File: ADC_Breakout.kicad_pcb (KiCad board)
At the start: 2 copper layers, 40.1 x 35.2 mm, 25 parts, among them J1 Analog Pins, J2 Digital Power, J3 Clock Chooser, J4 Analog Power, J5 SPI Communication, U1 ADS131M08QPBSRQ1, U2 SN74AUP2G80DCUR, X1 SIT8924BA-22-33E-8.192000, Y1 Crystal_Small

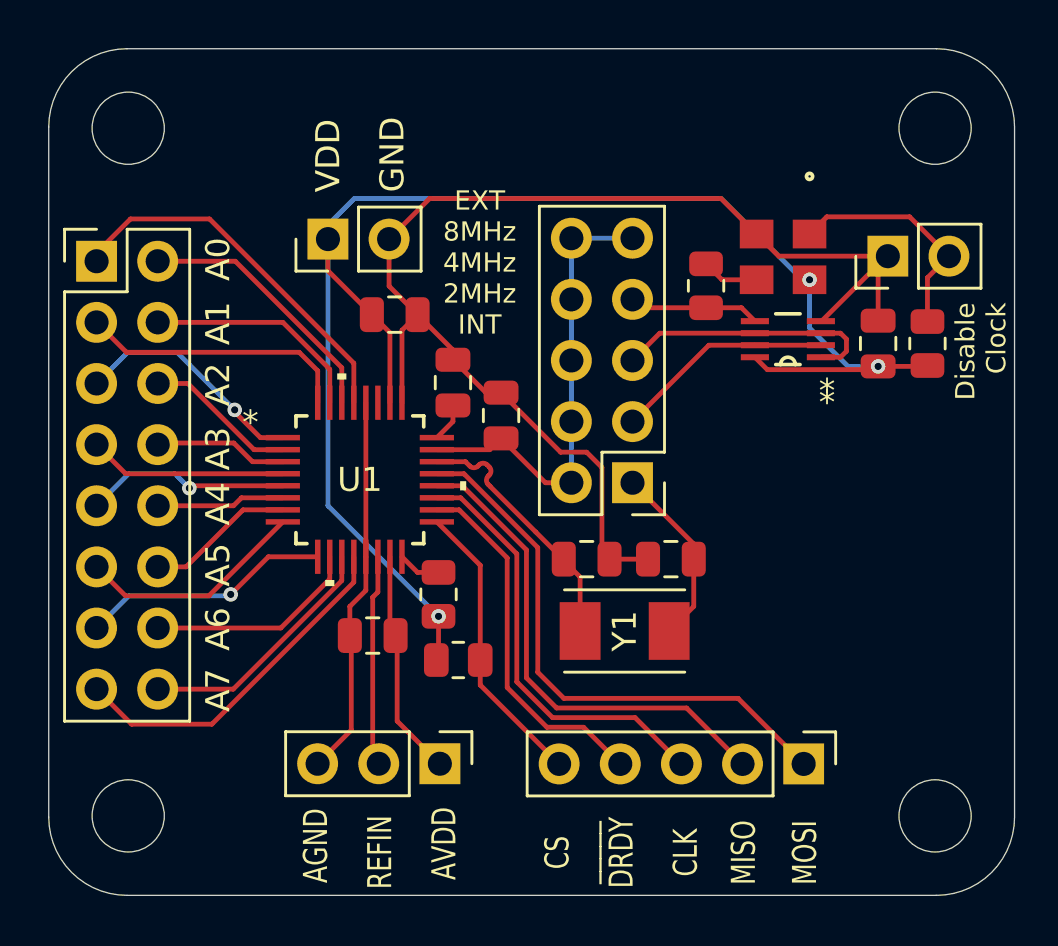
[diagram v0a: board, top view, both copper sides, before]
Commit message: Updated explanations for headers
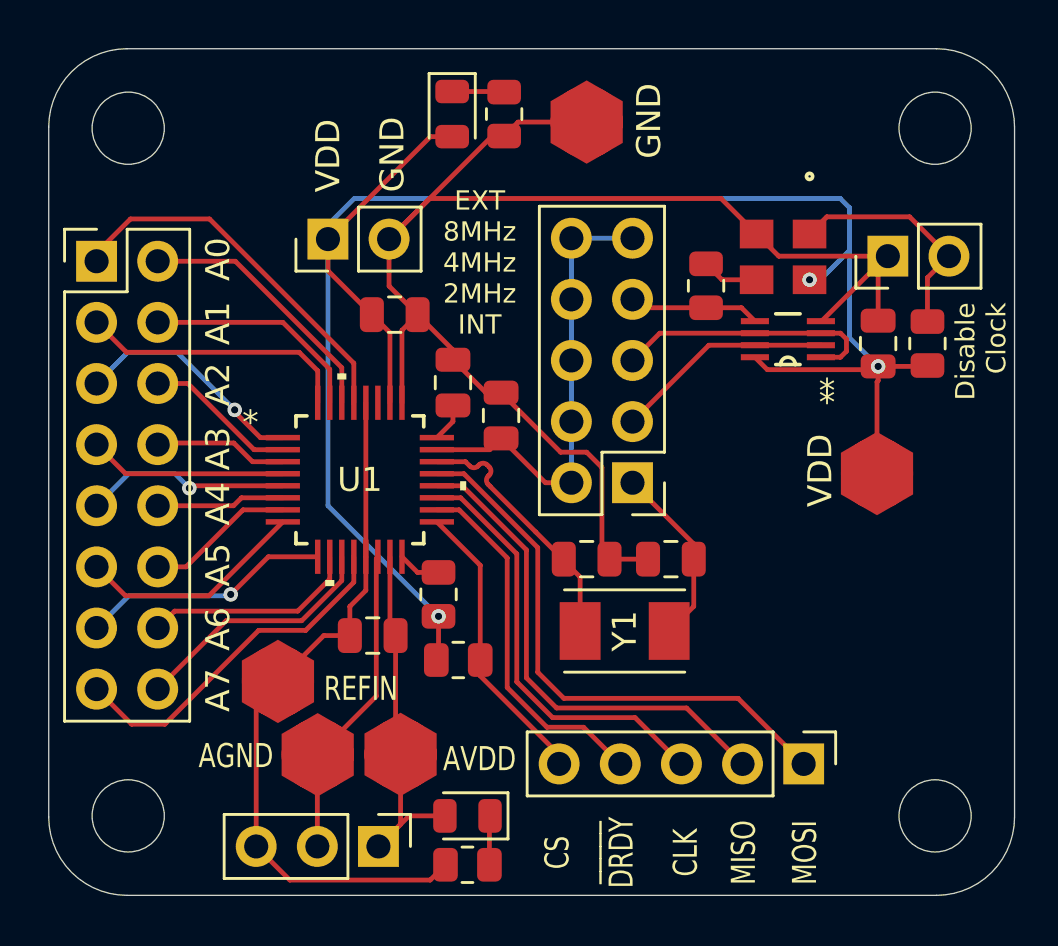
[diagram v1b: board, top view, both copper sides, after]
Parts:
- added D1: LED, LED_SMD:LED_0805_2012Metric, F.Cu at (40.8, 28.2)
- added D2: LED, LED_SMD:LED_0805_2012Metric, F.Cu at (41.4, 57.4)
- added R5: 500, Resistor_SMD:R_0805_2012Metric, F.Cu at (42.9, 28.2)
- added R6: 500, Resistor_SMD:R_0805_2012Metric, F.Cu at (41.4, 59.4)
- added TP1: TestPoint, SVT_Special:TestPoint_HEX_3mmID, F.Cu at (58.4, 43.2)
- added TP2: TestPoint, SVT_Special:TestPoint_HEX_3mmID, F.Cu at (38.6, 54.8)
- added TP3: TestPoint, SVT_Special:TestPoint_HEX_3mmID, F.Cu at (46.4, 28.6)
- added TP4: TestPoint, SVT_Special:TestPoint_HEX_3mmID, F.Cu at (33.5, 51.8)
- added TP5: TestPoint, SVT_Special:TestPoint_HEX_3mmID, F.Cu at (35.2, 54.9)
- moved J4 4.28 mm to (37.7, 58.7)
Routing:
- net VDD: track 62.7 -> 78.4 mm
- net GNDA: track 15.9 -> 29.7 mm
- net GND: track 52.8 -> 63.0 mm
- net VDDA: track 9.46 -> 15.9 mm
- net /REFIN: track 8.79 -> 13.1 mm
- net Net-(D1-K): track 0.00 -> 2.17 mm
- net Net-(D2-K): track 0.00 -> 2.04 mm

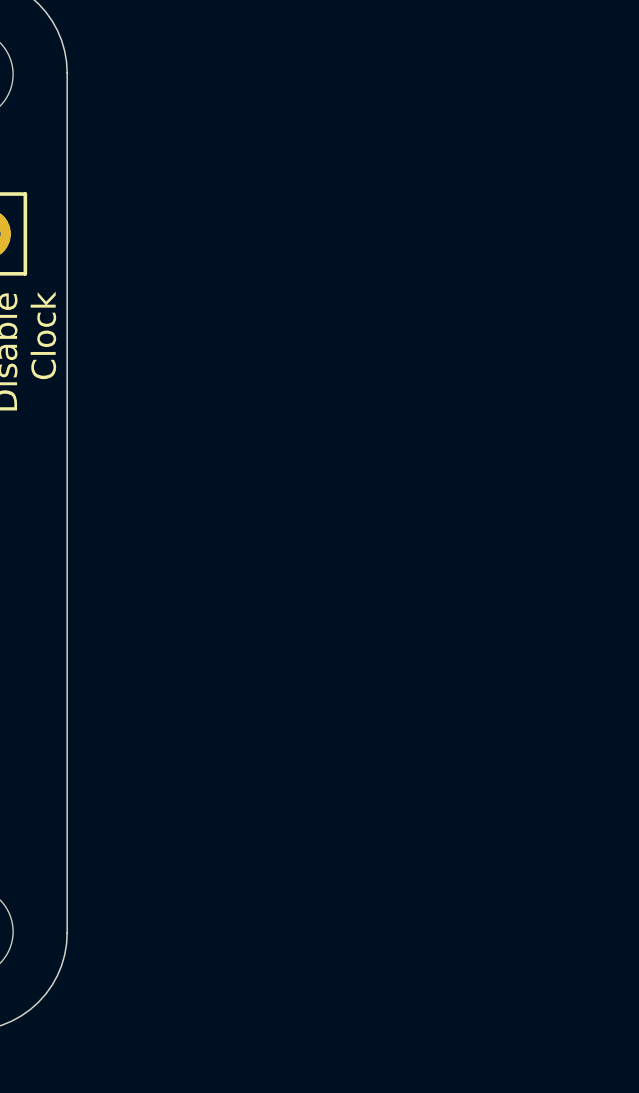
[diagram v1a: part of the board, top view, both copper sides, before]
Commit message: Updated schematic with antialiasing
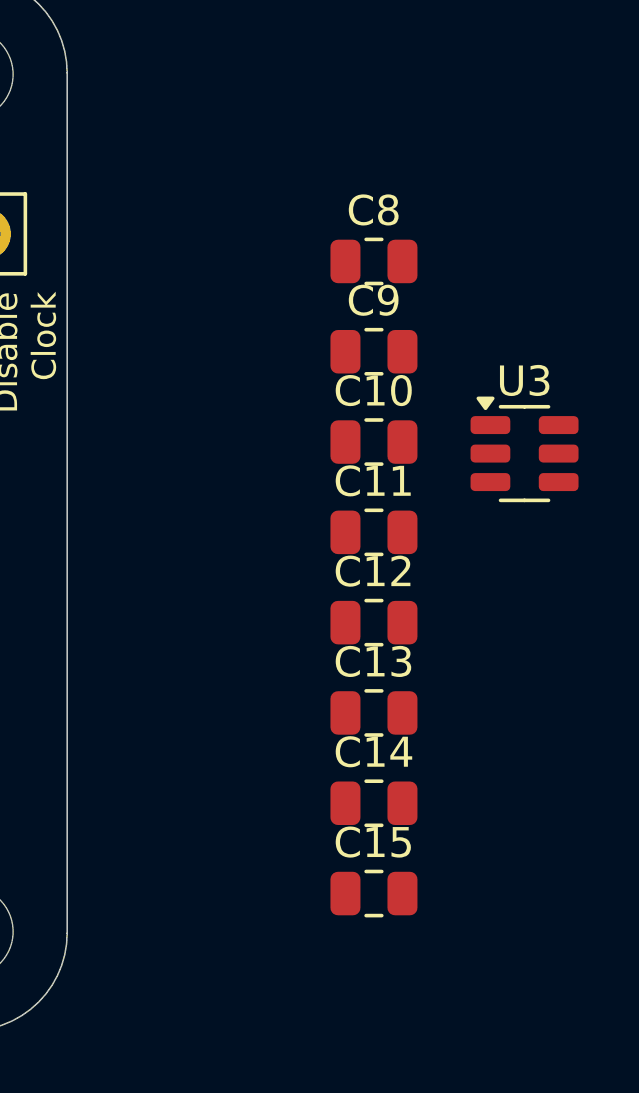
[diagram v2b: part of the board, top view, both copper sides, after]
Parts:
- added C10: 1000p, Capacitor_SMD:C_0805_2012Metric, F.Cu at (74.4, 41.1)
- added C11: 1000p, Capacitor_SMD:C_0805_2012Metric, F.Cu at (74.4, 44.1)
- added C12: 1000p, Capacitor_SMD:C_0805_2012Metric, F.Cu at (74.4, 47.1)
- added C13: 1000p, Capacitor_SMD:C_0805_2012Metric, F.Cu at (74.4, 50.1)
- added C14: 1000p, Capacitor_SMD:C_0805_2012Metric, F.Cu at (74.4, 53.1)
- added C15: 1000p, Capacitor_SMD:C_0805_2012Metric, F.Cu at (74.4, 56.1)
- added C8: 1000p, Capacitor_SMD:C_0805_2012Metric, F.Cu at (74.4, 35.1)
- added C9: 1000p, Capacitor_SMD:C_0805_2012Metric, F.Cu at (74.4, 38.1)
- added U3: WE-TVS-824015043, Package_TO_SOT_SMD:SOT-23-6, F.Cu at (79.4, 41.5)

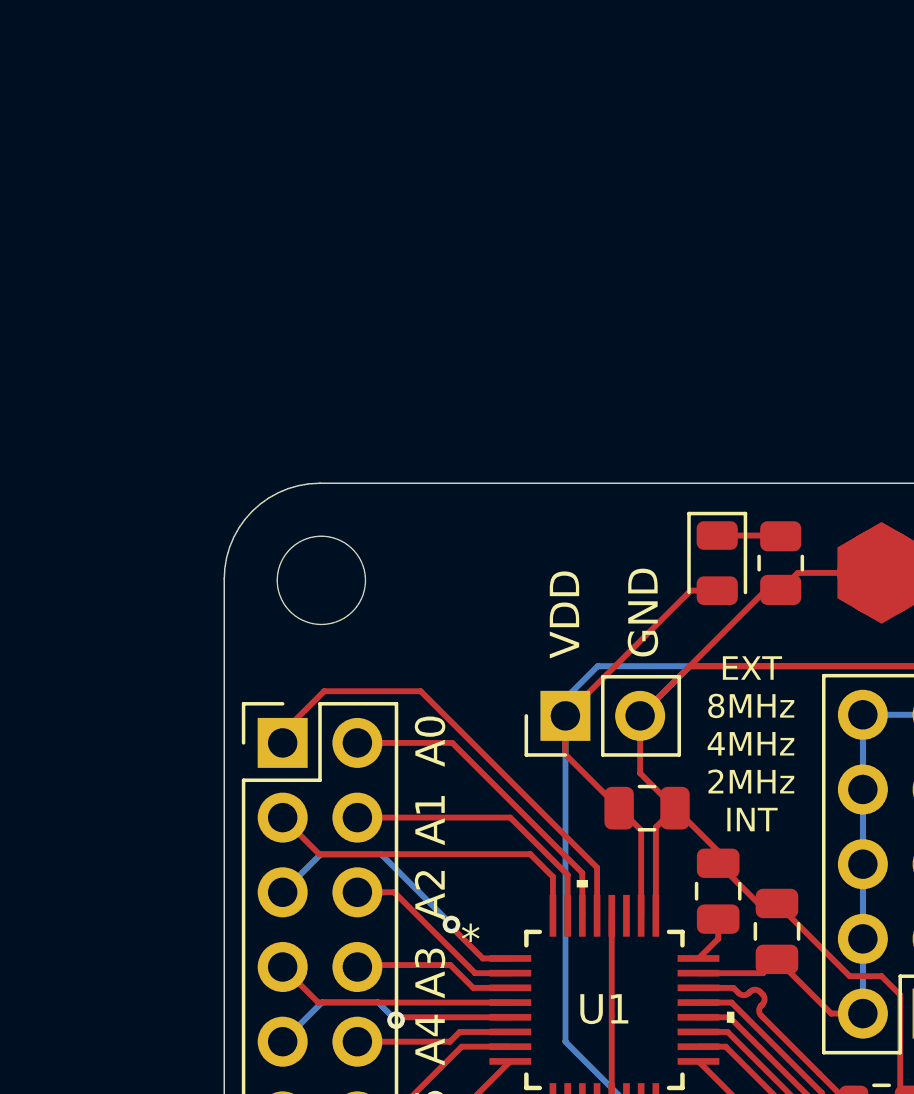
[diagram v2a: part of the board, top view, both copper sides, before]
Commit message: New footprints added
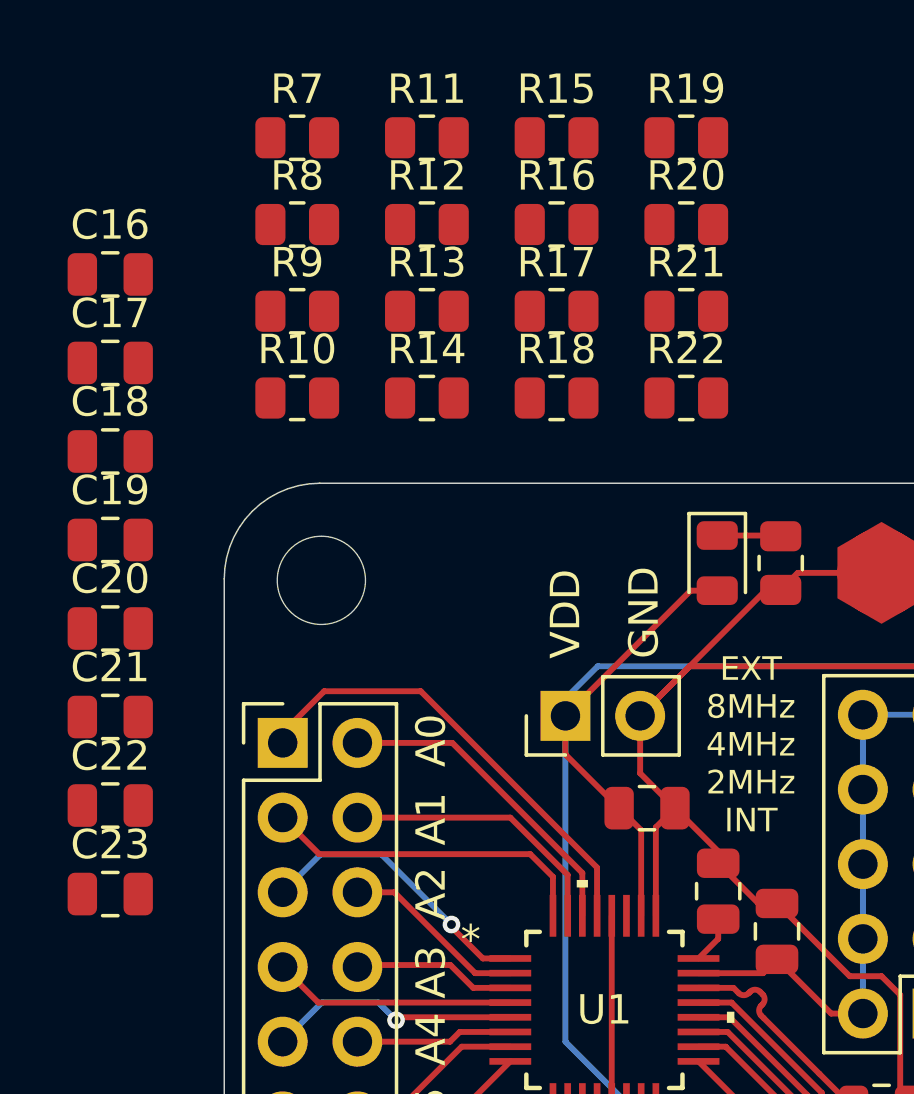
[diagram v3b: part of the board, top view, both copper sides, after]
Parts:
- added C16: 1000p, Capacitor_SMD:C_0805_2012Metric, F.Cu at (20.1, 18.4)
- added C17: 1000p, Capacitor_SMD:C_0805_2012Metric, F.Cu at (20.1, 21.4)
- added C18: 1000p, Capacitor_SMD:C_0805_2012Metric, F.Cu at (20.1, 24.4)
- added C19: 1000p, Capacitor_SMD:C_0805_2012Metric, F.Cu at (20.1, 27.5)
- added C20: 1000p, Capacitor_SMD:C_0805_2012Metric, F.Cu at (20.1, 30.5)
- added C21: 1000p, Capacitor_SMD:C_0805_2012Metric, F.Cu at (20.1, 33.5)
- added C22: 1000p, Capacitor_SMD:C_0805_2012Metric, F.Cu at (20.1, 36.5)
- added C23: 1000p, Capacitor_SMD:C_0805_2012Metric, F.Cu at (20.1, 39.5)
- added R10: 50, Resistor_SMD:R_0805_2012Metric, F.Cu at (26.5, 22.6)
- added R11: 50, Resistor_SMD:R_0805_2012Metric, F.Cu at (30.9, 13.8)
- added R12: 50, Resistor_SMD:R_0805_2012Metric, F.Cu at (30.9, 16.7)
- added R13: 50, Resistor_SMD:R_0805_2012Metric, F.Cu at (30.9, 19.7)
- added R14: 50, Resistor_SMD:R_0805_2012Metric, F.Cu at (30.9, 22.6)
- added R15: 50, Resistor_SMD:R_0805_2012Metric, F.Cu at (35.3, 13.8)
- added R16: 50, Resistor_SMD:R_0805_2012Metric, F.Cu at (35.3, 16.7)
- added R17: 50, Resistor_SMD:R_0805_2012Metric, F.Cu at (35.3, 19.7)
- added R18: 50, Resistor_SMD:R_0805_2012Metric, F.Cu at (35.3, 22.6)
- added R19: 50, Resistor_SMD:R_0805_2012Metric, F.Cu at (39.7, 13.8)
- added R20: 50, Resistor_SMD:R_0805_2012Metric, F.Cu at (39.7, 16.7)
- added R21: 50, Resistor_SMD:R_0805_2012Metric, F.Cu at (39.7, 19.7)
- added R22: 50, Resistor_SMD:R_0805_2012Metric, F.Cu at (39.7, 22.6)
- added R7: 50, Resistor_SMD:R_0805_2012Metric, F.Cu at (26.5, 13.8)
- added R8: 50, Resistor_SMD:R_0805_2012Metric, F.Cu at (26.5, 16.7)
- added R9: 50, Resistor_SMD:R_0805_2012Metric, F.Cu at (26.5, 19.7)
- C1: value 220n -> 1u
- C2: value 1u -> 220n
- C3: value 1u -> 10p
- C5: value 10p -> 1u
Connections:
- net /NSYNC renamed /ADC/NSYNC
- C1 pad 1: Net-(U1-CAP) -> VDD
- C2 pad 1: VDD -> Net-(U1-CAP)
- C3 pad 1: VDDA -> /CLKIN
- C3 pad 2: GNDA -> GND
- C5 pad 1: /CLKIN -> VDDA
- C5 pad 2: GND -> GNDA
- U1 pad 1: /A2_P -> /ADC/FA2_P
- U1 pad 10: /A6_N -> /ADC/FA6_N
- U1 pad 11: /A7_N -> /ADC/FA7_N
- U1 pad 12: /A7_P -> /ADC/FA7_P
- U1 pad 2: /A2_N -> /ADC/FA2_N
- U1 pad 29: /A0_P -> /ADC/FA0_P
- U1 pad 3: /A3_N -> /ADC/FA3_N
- U1 pad 30: /A0_N -> /ADC/FA0_N
- U1 pad 31: /A1_N -> /ADC/FA1_N
- U1 pad 32: /A1_P -> /ADC/FA1_P
- U1 pad 4: /A3_P -> /ADC/FA3_P
- U1 pad 5: /A4_P -> /ADC/FA4_P
- U1 pad 6: /A4_N -> /ADC/FA4_N
- U1 pad 7: /A5_N -> /ADC/FA5_N
- U1 pad 8: /A5_P -> /ADC/FA5_P
- U1 pad 9: /A6_P -> /ADC/FA6_P

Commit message: added all files
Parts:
- removed C10, C11, C12, C13, C14, C15, C8, C9: 1000p, Capacitor_SMD:C_0805_2012Metric
- removed U3: WE-TVS-824015043, Package_TO_SOT_SMD:SOT-23-6
- added SW1: SW_MEC_5E, SMD_Button:SW_B3SL-1002P_OMR, F.Cu at (151.2, 15.1)
- C16, C17, C18, C19, C20, C21, C22, C23, R10, R11, R12, R13, R14, R15, R16, R17, R18, R19, R20, R21, R22, R7, R8, R9: moved to B.Cu
- moved C3 96.1 mm to (133.5, 47.1)
- moved C6 96.1 mm to (145.9, 43.9)
- moved C7 96.1 mm to (142.4, 43.9)
- moved D1 96.1 mm to (136.8, 25.4)
- moved H1 96.1 mm to (123.4, 26.0)
- moved H2 96.1 mm to (156.9, 26.0)
- moved H3 96.1 mm to (123.4, 54.5)
- moved H4 96.1 mm to (156.9, 54.5)
- moved J3 96.1 mm to (144.3, 40.7)
- moved JP1 96.1 mm to (154.9, 31.3)
- moved TP2 96.1 mm to (134.7, 52.0)
- moved TP3 96.1 mm to (142.4, 25.7)
- moved TP4 96.1 mm to (129.6, 49.0)
- moved TP5 96.1 mm to (131.3, 52.0)
- moved U2 96.1 mm to (150.8, 34.7)
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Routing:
- net /A0_P: track 15.7 -> 0.00 mm
- net /A7_P: track 14.8 -> 0.00 mm
- net /A1_P: track 11.3 -> 0.00 mm
- net /A0_N: track 10.9 -> 0.00 mm
- net /A7_N: track 10.5 -> 0.00 mm
- net /A6_P: track 10.4 -> 0.00 mm, vias 1 -> 0
- net /A2_P: track 9.79 -> 0.00 mm, vias 1 -> 0
- net /A5_P: track 9.51 -> 0.00 mm
- net /A1_N: track 9.35 -> 0.00 mm
- net /A6_N: track 8.92 -> 0.00 mm
- net /A4_P: track 8.59 -> 0.00 mm, vias 1 -> 0
- net /A3_P: track 8.24 -> 0.00 mm
- net /A2_N: track 6.34 -> 0.00 mm
- net /A5_N: track 6.18 -> 0.00 mm
- net /A3_N: track 5.55 -> 0.00 mm
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
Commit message: Updated Layout
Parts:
- removed J1: Analog Pins, Connector_PinHeader_2.54mm:PinHeader_2x08_P2.54mm_Vertical
- removed J5: SPI Communication, Connector_PinHeader_2.54mm:PinHeader_1x05_P2.54mm_Vertical
- added D0: D_TVS_Small, Capacitor_SMD:C_0603_1608Metric_Pad1.08x0.95mm_HandSolder, F.Cu at (142.2, 84.7)
- added J0: Conn_01x06, Connector_PinHeader_2.54mm:PinHeader_1x06_P2.54mm_Vertical, F.Cu at (156.0, 104.1)
- added J10: Conn_01x02, Connector_PinHeader_2.54mm:PinHeader_1x02_P2.54mm_Vertical, F.Cu at (114.7, 104.8)
- added J11: Conn_01x02, Connector_PinHeader_2.54mm:PinHeader_1x02_P2.54mm_Vertical, F.Cu at (114.7, 115.6)
- added J12: Conn_01x02, Connector_PinHeader_2.54mm:PinHeader_1x02_P2.54mm_Vertical, F.Cu at (121.4, 123.4)
- added J13: Conn_01x02, Connector_PinHeader_2.54mm:PinHeader_1x02_P2.54mm_Vertical, F.Cu at (132.8, 123.5)
- added J6: Conn_01x02, Connector_PinHeader_2.54mm:PinHeader_1x02_P2.54mm_Vertical, F.Cu at (133.0, 81.9)
- added J7: Conn_01x02, Connector_PinHeader_2.54mm:PinHeader_1x02_P2.54mm_Vertical, F.Cu at (122.0, 81.9)
- added J8: Conn_01x02, Connector_PinHeader_2.54mm:PinHeader_1x02_P2.54mm_Vertical, F.Cu at (114.7, 88.5)
- added J9: Conn_01x02, Connector_PinHeader_2.54mm:PinHeader_1x02_P2.54mm_Vertical, F.Cu at (114.7, 99.2)
- C16, C17, C18, C19, C20, C21, C22, C23, R10, R11, R12, R13, R14, R15, R16, R17, R18, R19, R20, R21, R22, R7, R8, R9: moved to F.Cu
- moved SW1 101.7 mm to (146.1, 116.6), turned to 90 degrees
- moved H1 101.1 mm to (113.0, 126.5)
- moved H2 100.6 mm to (160.0, 126.5)
- moved R20 80.9 mm to (132.7, 119.9), turned to 90 degrees
- moved TP4 78.5 mm to (153.2, 123.8)
- moved R22 78.3 mm to (130.7, 119.9), turned to 90 degrees
- moved R7 74.6 mm to (132.7, 85.5), turned to -90 degrees
- moved R19 74.3 mm to (121.5, 119.9), turned to 90 degrees
- moved TP5 74.1 mm to (149.6, 123.8), turned to 180 degrees
- moved TP3 73.9 mm to (154.1, 98.7)
- moved R21 73.6 mm to (123.6, 119.9), turned to 90 degrees
- moved C5 72.6 mm to (136.5, 110.5), turned to 180 degrees
- moved R16 72.5 mm to (118.2, 115.4)
- moved R8 71.8 mm to (130.7, 85.5), turned to -90 degrees
- moved C23 70.8 mm to (132.9, 110.5), turned to 0 degrees
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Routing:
- net VDD: track 80.0 -> 23.1 mm, vias 3 -> 0
- net GND: track 63.0 -> 25.4 mm, vias 0 -> 8
- net GNDA: track 29.7 -> 60.3 mm, vias 0 -> 1
- net /ADC/NSYNC: track 1.79 -> 24.3 mm
- net VDDA: track 15.9 -> 36.9 mm
- net /CS: track 12.2 -> 32.9 mm, vias 0 -> 2
- net /ADC/FA2_P: track 0.00 -> 17.4 mm
- net /ADC/FA6_P: track 0.00 -> 17.3 mm
- net /ADC/FA1_P: track 0.00 -> 17.2 mm
- net /REFIN: track 13.1 -> 30.1 mm
- net /ADC/FA2_N: track 0.00 -> 16.7 mm
- net /ADC/FA6_N: track 0.00 -> 16.7 mm
- net /ADC/FA5_P: track 0.00 -> 16.6 mm
- net /ADC/FA1_N: track 0.00 -> 16.4 mm
- net /ADC/FA5_N: track 0.00 -> 15.9 mm
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- added copper zone on F.Cu, net /CLKIN
- added copper zone on B.Cu, net GND
- added copper zone on F.Cu, net VDD
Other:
- board size 40.1 x 35.2 mm -> 55 x 55 mm
- board text added: "+"
- board text added: "-"
- board text added: "2MHz"
- board text added: "4MHz"
- board text added: "8MHz"
- board text added: "APWR"
- board text added: "DPWR"
- board text added: "Ext"
- board text added: "GNDA"
- board text added: "Int"
- board text added: "No Fill Under Clocks"
- board text added: "REF"
- board text added: "RESET"
- board text added: "VDDA"
- board text removed: "AGND"
- board text removed: "AVDD"
- board text removed: "EXT 8MHz 4MHz 2MHz INT"

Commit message: Updated Layout
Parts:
- moved TP4 14.8 mm to (142.4, 113.7)
- moved TP5 11.4 mm to (140.7, 116.7)
- moved SW1 9.24 mm to (152.1, 123.6)
- moved TP2 8.28 mm to (144.2, 116.7)
- moved R6 6.26 mm to (147.0, 116.8)
- moved R3 5.56 mm to (155.2, 90.5), turned to -90 degrees
- moved C6 5.48 mm to (148.3, 103.1), turned to -90 degrees
- moved JP1 3.82 mm to (155.3, 84.2)
- moved C7 3.05 mm to (140.1, 102.3)
- moved C3 2.99 mm to (140.1, 98.8)
- moved R2 2.80 mm to (149.0, 110.2), turned to 90 degrees
- moved D1 2.79 mm to (147.6, 79.7)
- moved R5 2.79 mm to (147.6, 81.9)
- moved D2 2.55 mm to (149.0, 116.8)
- moved C1 2.32 mm to (134.8, 96.5), turned to 90 degrees
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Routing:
- net VDD: track 23.1 -> 6.63 mm
- net GNDA: track 60.3 -> 45.6 mm, vias 1 -> 2
- net GND: track 25.4 -> 10.7 mm, vias 8 -> 11
- net /MOSI: track 29.2 -> 21.1 mm, vias 1 -> 0
- net /ADC/NSYNC: track 24.3 -> 31.9 mm
- net /MISO: track 29.4 -> 22.0 mm, vias 1 -> 0
- net /CS: track 32.9 -> 26.6 mm, vias 2 -> 0
- net /CLK: track 28.2 -> 22.8 mm, vias 1 -> 0
- net Net-(JP1-B): track 9.81 -> 5.29 mm
- net /*DRDY: track 28.6 -> 24.8 mm, vias 1 -> 0
- net /XTAL2: track 8.82 -> 6.41 mm
- net /4MHz: track 11.1 -> 8.79 mm
- net /INT_OSC: track 9.83 -> 7.67 mm
- net /REFIN: track 30.1 -> 28.2 mm, vias 0 -> 1
- net /CLKIN: track 3.67 -> 5.53 mm
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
